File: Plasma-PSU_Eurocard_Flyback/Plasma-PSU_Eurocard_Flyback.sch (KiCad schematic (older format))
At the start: 0 parts

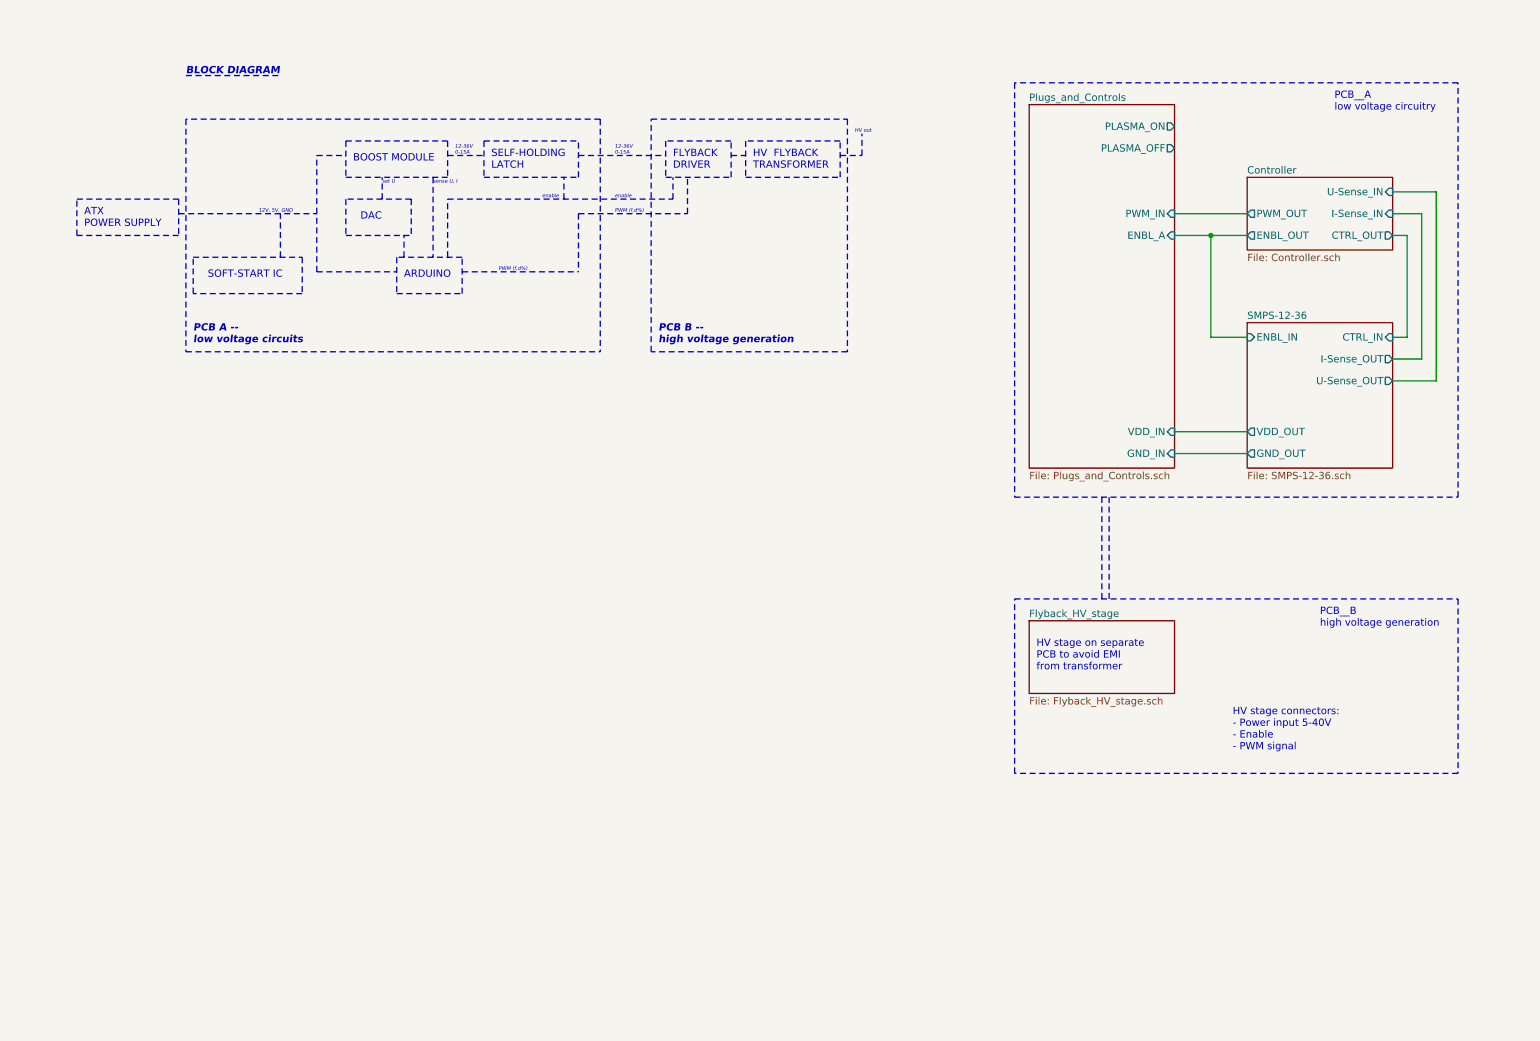
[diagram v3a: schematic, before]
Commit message: DAC sets U_out
DAC converter in SMPS sheet sets boost modules output voltage.
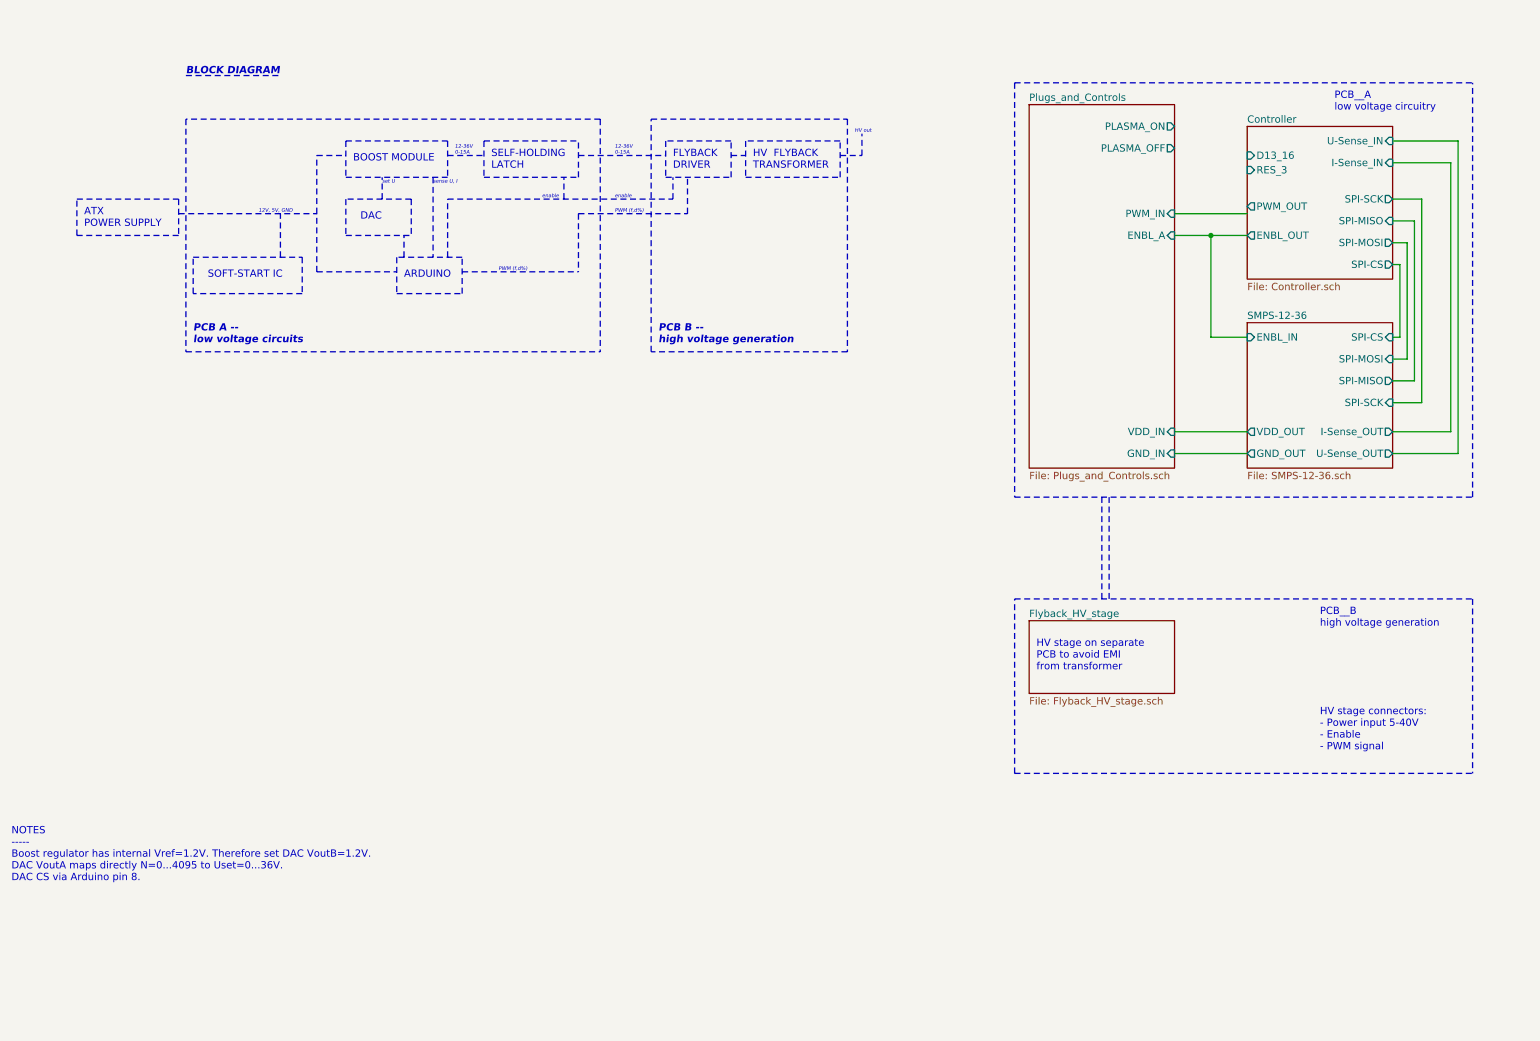
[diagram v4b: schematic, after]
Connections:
- wire segments 16 -> 25
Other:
- note added: "NOTES\n-----\nBoost regulator has internal Vref=1.2V. Therefore set DAC VoutB=1.2V.\nDAC VoutA maps directly N=0...4095 to Uset=0...36V.\nDAC CS via Arduino pin 8."
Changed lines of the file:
@@
 	9200 2250 8950 2250
 $Sheet
-S 9200 1850 1000 500
+S 9200 1500 1000 1050
 U 5E8B09E3
 F0 "Controller" 50
 F1 "Controller.sch" 50
-F2 "CTRL_OUT" O R 10200 2250 50
-F3 "ENBL_OUT" O L 9200 2250 50
-F4 "I-Sense_IN" I R 10200 2100 50
-F5 "U-Sense_IN" I R 10200 1950 50
-F6 "PWM_OUT" O L 9200 2100 50
+F2 "ENBL_OUT" O L 9200 2250 50
+F3 "I-Sense_IN" I R 10200 1750 50
+F4 "U-Sense_IN" I R 10200 1600 50
+F5 "PWM_OUT" O L 9200 2050 50
+F6 "RES_3" I L 9200 1800 50
+F7 "D13_16" I L 9200 1700 50
+F8 "SPI-SCK" O R 10200 2000 50
+F9 "SPI-MISO" I R 10200 2150 50
+F10 "SPI-MOSI" O R 10200 2300 50
+F11 "SPI-CS" O R 10200 2450 50
 $EndSheet
 Wire Wire Line
@@
 Wire Wire Line
 	8950 2250 8700 2250
-Wire Wire Line
-	10200 2250 10300 2250
-Wire Wire Line
-	10300 2250 10300 2950
-Wire Wire Line
-	10300 2950 10200 2950
-Wire Wire Line
-	10200 2100 10400 2100
-Wire Wire Line
-	10400 2100 10400 3100
-Wire Wire Line
-	10400 3100 10200 3100
-Wire Wire Line
-	10200 1950 10500 1950
-Wire Wire Line
-	10500 1950 10500 3250
-Wire Wire Line
-	10500 3250 10200 3250
 Wire Notes Line
 	7600 1200 7600 4050
 Wire Notes Line
-	10650 4050 10650 1200
-Wire Notes Line
-	10650 1200 7600 1200
-Wire Notes Line
-	7600 4050 10650 4050
-Text Notes 9100 5800 0    50   ~ 0
+	10750 4050 10750 1200
+Text Notes 9700 5800 0    50   ~ 0
 HV stage connectors:\n- Power input 5-40V\n- Enable\n- PWM signal
 Text Notes 7750 5250 0    50   ~ 0
@@
 $EndSheet
 Wire Notes Line
-	7600 4750 10650 4750
-Wire Notes Line
-	10650 4750 10650 5950
-Wire Notes Line
-	10650 5950 7600 5950
+	10750 4750 10750 5950
 Wire Notes Line
 	7600 5950 7600 4750
@@
 F2 "VDD_OUT" O L 9200 3600 50
 F3 "GND_OUT" O L 9200 3750 50
-F4 "CTRL_IN" I R 10200 2950 50
-F5 "ENBL_IN" I L 9200 2950 50
-F6 "I-Sense_OUT" O R 10200 3100 50
-F7 "U-Sense_OUT" O R 10200 3250 50
+F4 "ENBL_IN" I L 9200 2950 50
+F5 "I-Sense_OUT" O R 10200 3600 50
+F6 "U-Sense_OUT" O R 10200 3750 50
+F7 "SPI-SCK" I R 10200 3400 50
+F8 "SPI-MISO" O R 10200 3250 50
+F9 "SPI-MOSI" I R 10200 3100 50
+F10 "SPI-CS" I R 10200 2950 50
 $EndSheet
 Text Notes 1200 2200 0    50   ~ 0
@@
 Wire Notes Line
 	2800 2500 2800 2100
+Wire Wire Line
+	10200 2950 10250 2950
+Wire Wire Line
+	10250 2950 10250 2450
+Wire Wire Line
+	10250 2450 10200 2450
+Wire Wire Line
+	10200 3100 10300 3100
+Wire Wire Line
+	10300 3100 10300 2300
+Wire Wire Line
+	10300 2300 10200 2300
+Wire Wire Line
+	10200 3250 10350 3250
+Wire Wire Line
+	10350 3250 10350 2150
+Wire Wire Line
+	10350 2150 10200 2150
+Wire Wire Line
+	10200 3400 10400 3400
+Wire Wire Line
+	10400 3400 10400 2000
+Wire Wire Line
+	10400 2000 10200 2000
+Wire Wire Line
+	10600 3600 10600 1750
+Wire Wire Line
+	10200 1750 10600 1750
+Wire Wire Line
+	10200 3600 10600 3600
+Wire Wire Line
+	10650 3750 10650 1600
+Wire Wire Line
+	10200 1600 10650 1600
+Wire Wire Line
+	10200 3750 10650 3750
+Wire Notes Line
+	7600 1200 10750 1200
+Wire Notes Line
+	7600 4050 10750 4050
+Wire Notes Line
+	7600 4750 10750 4750
+Wire Notes Line
+	7600 5950 10750 5950
+Text Notes 700  6700 0    50   ~ 0
+NOTES\n-----\nBoost regulator has internal Vref=1.2V. Therefore set DAC VoutB=1.2V.\nDAC VoutA maps directly N=0...4095 to Uset=0...36V.\nDAC CS via Arduino pin 8.
 $EndSCHEMATC

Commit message: Datasheets included
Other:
- note added: "TODO SELECT SMPS FETS\nTODO SELECT SMPS SHUNT"
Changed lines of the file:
@@
 Text Notes 700  6700 0    50   ~ 0
 NOTES\n-----\nBoost regulator has internal Vref=1.2V. Therefore set DAC VoutB=1.2V.\nDAC VoutA maps directly N=0...4095 to Uset=0...36V.\nDAC CS via Arduino pin 8.
+Text Notes 800  4650 0    50   ~ 0
+TODO SELECT SMPS FETS\nTODO SELECT SMPS SHUNT
 $EndSCHEMATC

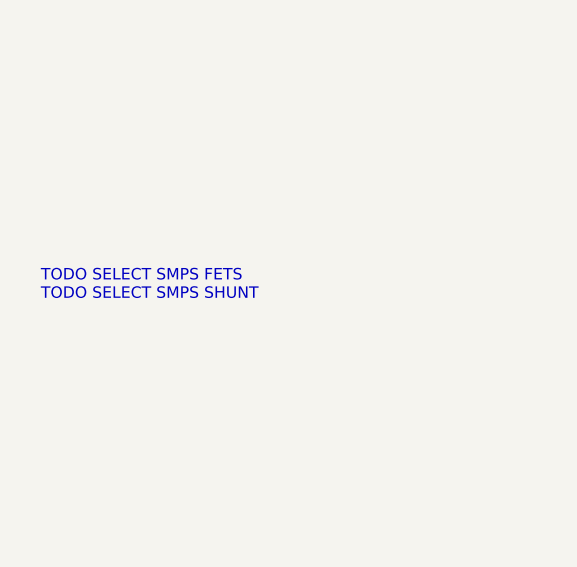
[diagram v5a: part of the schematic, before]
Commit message: SMPS & Shunt selected
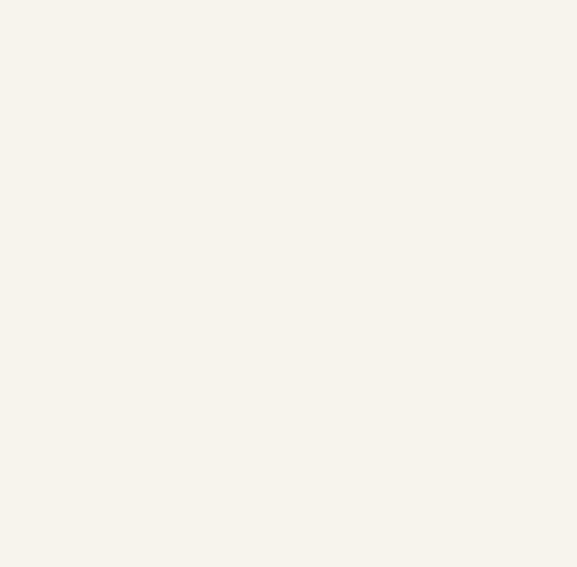
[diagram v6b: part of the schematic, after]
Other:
- note removed: "TODO SELECT SMPS FETS\nTODO SELECT SMPS SHUNT"
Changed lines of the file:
@@
 Text Notes 700  6700 0    50   ~ 0
 NOTES\n-----\nBoost regulator has internal Vref=1.2V. Therefore set DAC VoutB=1.2V.\nDAC VoutA maps directly N=0...4095 to Uset=0...36V.\nDAC CS via Arduino pin 8.
-Text Notes 800  4650 0    50   ~ 0
-TODO SELECT SMPS FETS\nTODO SELECT SMPS SHUNT
 $EndSCHEMATC

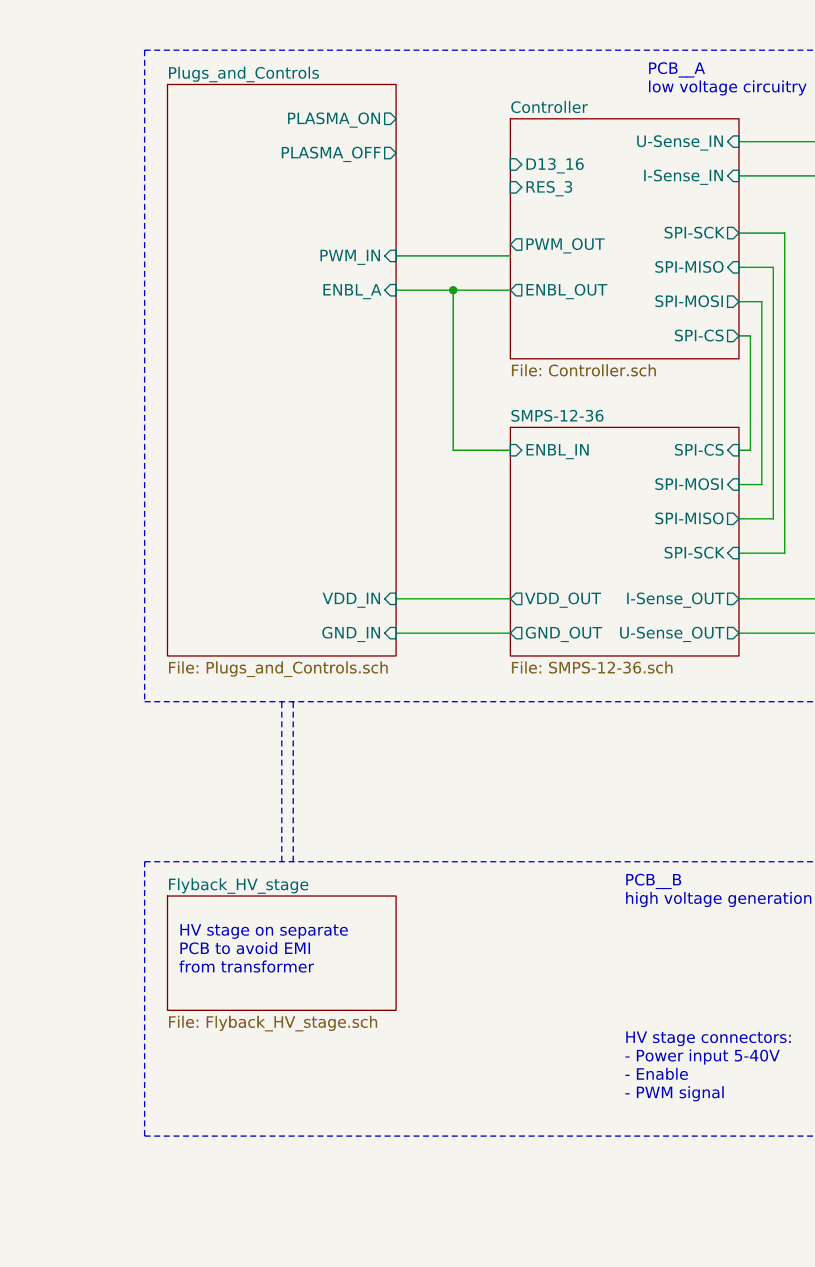
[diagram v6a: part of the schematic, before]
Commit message: Footprints added
All footprints included, except:
- Boost Inductor
- 60A fuse holder
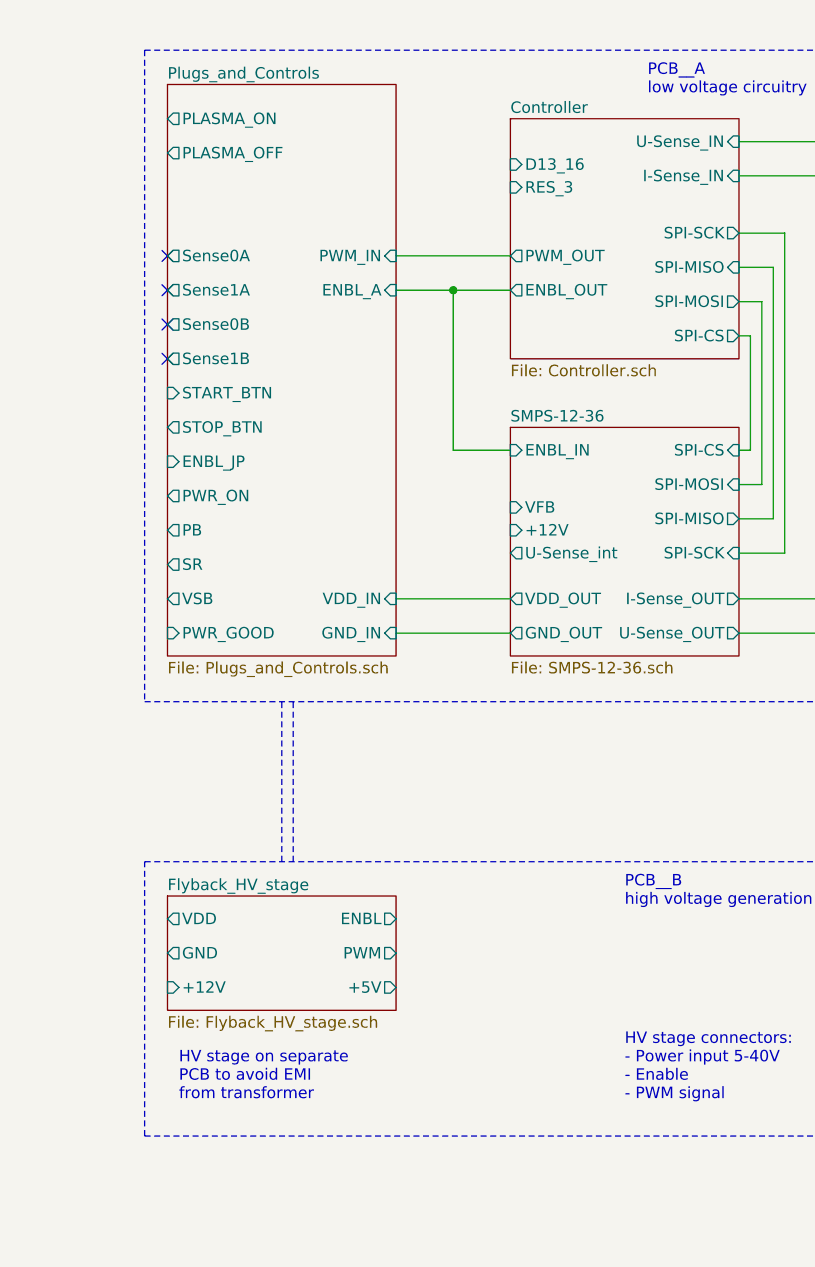
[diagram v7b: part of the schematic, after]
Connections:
- no-connect marks 0 -> 4
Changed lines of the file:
@@
 F0 "Plugs_and_Controls" 50
 F1 "Plugs_and_Controls.sch" 50
-F2 "PLASMA_ON" O R 8700 1500 50
-F3 "PLASMA_OFF" O R 8700 1650 50
+F2 "PLASMA_ON" O L 7700 1500 50
+F3 "PLASMA_OFF" O L 7700 1650 50
 F4 "ENBL_A" I R 8700 2250 50
 F5 "VDD_IN" I R 8700 3600 50
 F6 "GND_IN" I R 8700 3750 50
 F7 "PWM_IN" I R 8700 2100 50
+F8 "ENBL_JP" I L 7700 3000 50
+F9 "START_BTN" I L 7700 2700 50
+F10 "PWR_ON" O L 7700 3150 50
+F11 "PB" O L 7700 3300 50
+F12 "STOP_BTN" O L 7700 2850 50
+F13 "Sense0A" O L 7700 2100 50
+F14 "Sense1A" O L 7700 2250 50
+F15 "Sense0B" O L 7700 2400 50
+F16 "Sense1B" O L 7700 2550 50
+F17 "SR" O L 7700 3450 50
+F18 "VSB" O L 7700 3600 50
+F19 "PWR_GOOD" I L 7700 3750 50
 $EndSheet
 Wire Wire Line
@@
 F3 "I-Sense_IN" I R 10200 1750 50
 F4 "U-Sense_IN" I R 10200 1600 50
-F5 "PWM_OUT" O L 9200 2050 50
+F5 "PWM_OUT" O L 9200 2100 50
 F6 "RES_3" I L 9200 1800 50
 F7 "D13_16" I L 9200 1700 50
@@
 Text Notes 9700 5800 0    50   ~ 0
 HV stage connectors:\n- Power input 5-40V\n- Enable\n- PWM signal
-Text Notes 7750 5250 0    50   ~ 0
+Text Notes 7750 5800 0    50   ~ 0
 HV stage on separate \nPCB to avoid EMI \nfrom transformer
 $Sheet
@@
 F0 "Flyback_HV_stage" 50
 F1 "Flyback_HV_stage.sch" 50
+F2 "VDD" O L 7700 5000 50
+F3 "GND" O L 7700 5150 50
+F4 "ENBL" O R 8700 5000 50
+F5 "PWM" O R 8700 5150 50
+F6 "+12V" I L 7700 5300 50
+F7 "+5V" O R 8700 5300 50
 $EndSheet
 Wire Notes Line
@@
 F9 "SPI-MOSI" I R 10200 3100 50
 F10 "SPI-CS" I R 10200 2950 50
+F11 "+12V" I L 9200 3300 50
+F12 "VFB" I L 9200 3200 50
+F13 "U-Sense_int" O L 9200 3400 50
 $EndSheet
 Text Notes 1200 2200 0    50   ~ 0
@@
 Text Notes 700  6700 0    50   ~ 0
 NOTES\n-----\nBoost regulator has internal Vref=1.2V. Therefore set DAC VoutB=1.2V.\nDAC VoutA maps directly N=0...4095 to Uset=0...36V.\nDAC CS via Arduino pin 8.
+NoConn ~ 7700 2100
+NoConn ~ 7700 2250
+NoConn ~ 7700 2400
+NoConn ~ 7700 2550
 $EndSCHEMATC
